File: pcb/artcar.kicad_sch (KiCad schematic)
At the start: 28 parts, among them SW1 SW_SP3T

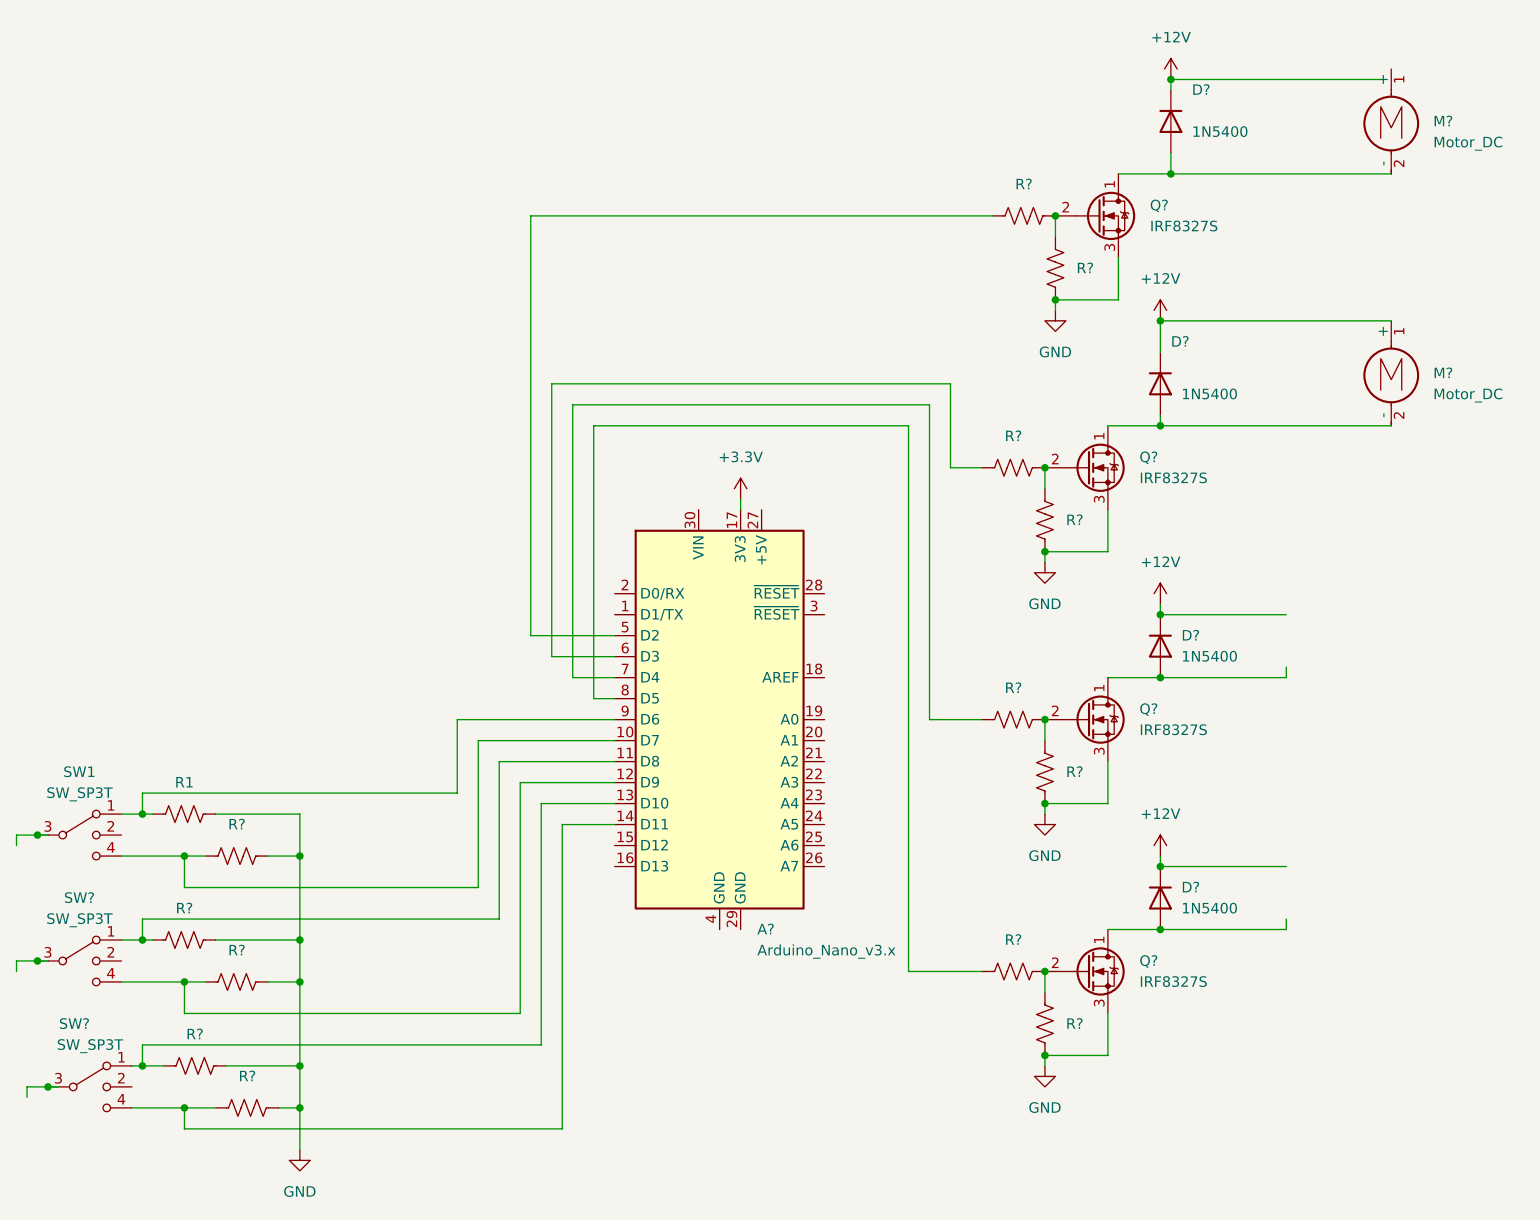
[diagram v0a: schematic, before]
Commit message: More update to the schematic
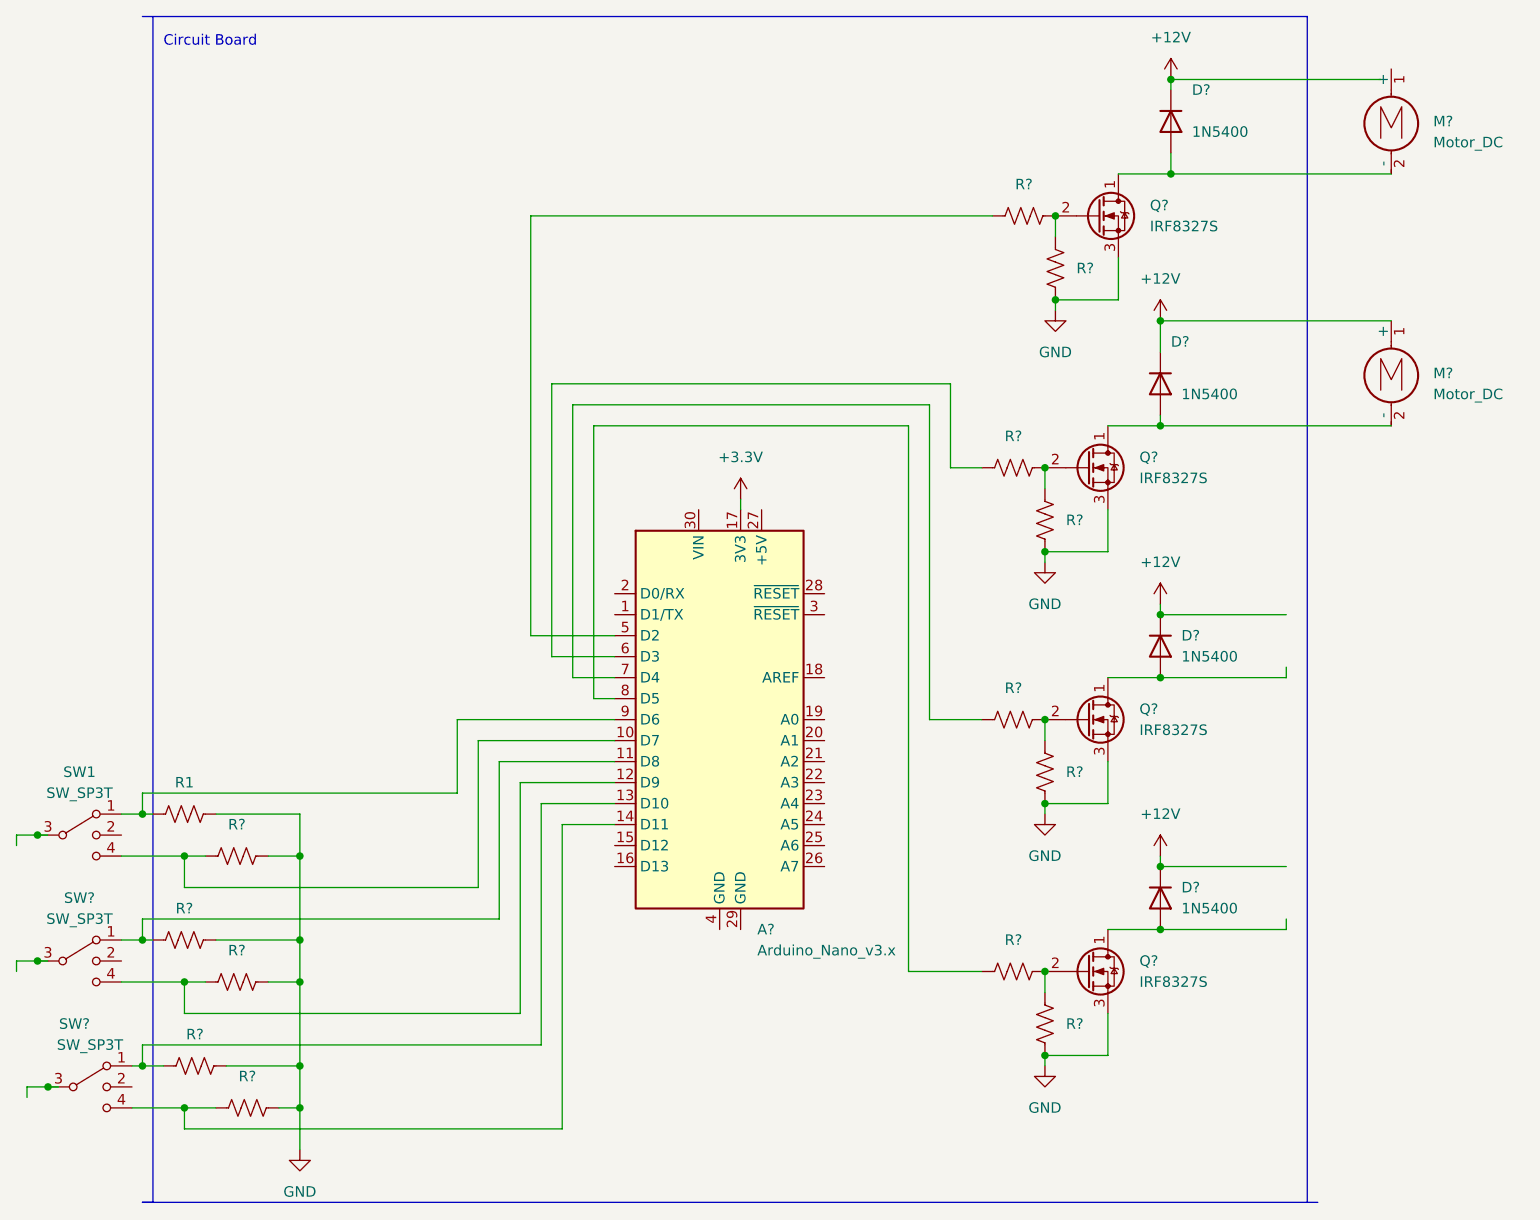
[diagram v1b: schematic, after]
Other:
- note added: "Circuit Board"
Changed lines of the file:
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@@
+    (stroke (width 0) (type default) (color 0 0 0 0))
+  )
+  (polyline (pts (xy 45.72 17.78) (xy 45.72 161.29))
     (stroke (width 0) (type default) (color 0 0 0 0))
   )
@@
     (stroke (width 0) (type default) (color 0 0 0 0))
   )
+  (polyline (pts (xy 185.42 161.29) (xy 185.42 17.78))
+    (stroke (width 0) (type default) (color 0 0 0 0))
+  )
   (wire (pts (xy 49.53 134.62) (xy 52.07 134.62))
     (stroke (width 0) (type default) (color 0 0 0 0))
@@
     (stroke (width 0) (type default) (color 0 0 0 0))
   )
+  (polyline (pts (xy 45.72 161.29) (xy 44.45 161.29))
+    (stroke (width 0) (type default) (color 0 0 0 0))
+  )
   (wire (pts (xy 44.45 111.76) (xy 82.55 111.76))
     (stroke (width 0) (type default) (color 0 0 0 0))
@@
     (stroke (width 0) (type default) (color 0 0 0 0))
   )
+  (polyline (pts (xy 44.45 17.78) (xy 185.42 17.78))
+    (stroke (width 0) (type default) (color 0 0 0 0))
+  )
   (wire (pts (xy 49.53 149.86) (xy 49.53 152.4))
     (stroke (width 0) (type default) (color 0 0 0 0))
@@
     (stroke (width 0) (type default) (color 0 0 0 0))
   )
+  (polyline (pts (xy 44.45 161.29) (xy 186.69 161.29))
+    (stroke (width 0) (type default) (color 0 0 0 0))
+  )
   (wire (pts (xy 153.67 102.87) (xy 153.67 105.41))
     (stroke (width 0) (type default) (color 0 0 0 0))
@@
     (stroke (width 0) (type default) (color 0 0 0 0))
   )
+  (text "Circuit Board" (at 46.99 21.59 0)
+    (effects (font (size 1.27 1.27)) (justify left bottom))
+  )
   (symbol (lib_id "Device:R_US") (at 151.13 41.91 90) (unit 1)
